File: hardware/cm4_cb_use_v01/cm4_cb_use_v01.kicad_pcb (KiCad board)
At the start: 2 copper layers, 60 x 55 mm, 21 parts, among them J1 DNP, J2 USB4105-GF-A, J3 SM04B-SRSS-TB(LF)(SN), J4 USB_OTG, U1 74LVC1G07SE-7, U2 TPD2EUSB30

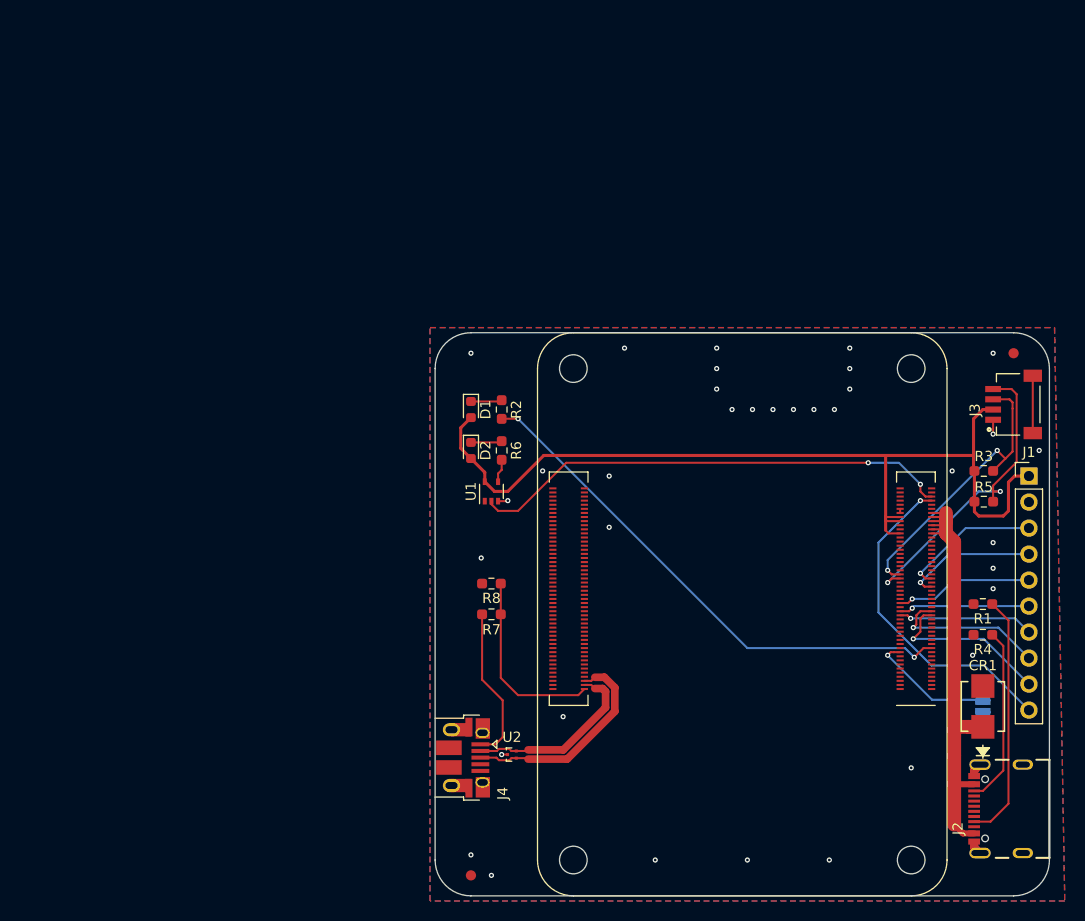
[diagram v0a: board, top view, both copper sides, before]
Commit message: added some 3d models
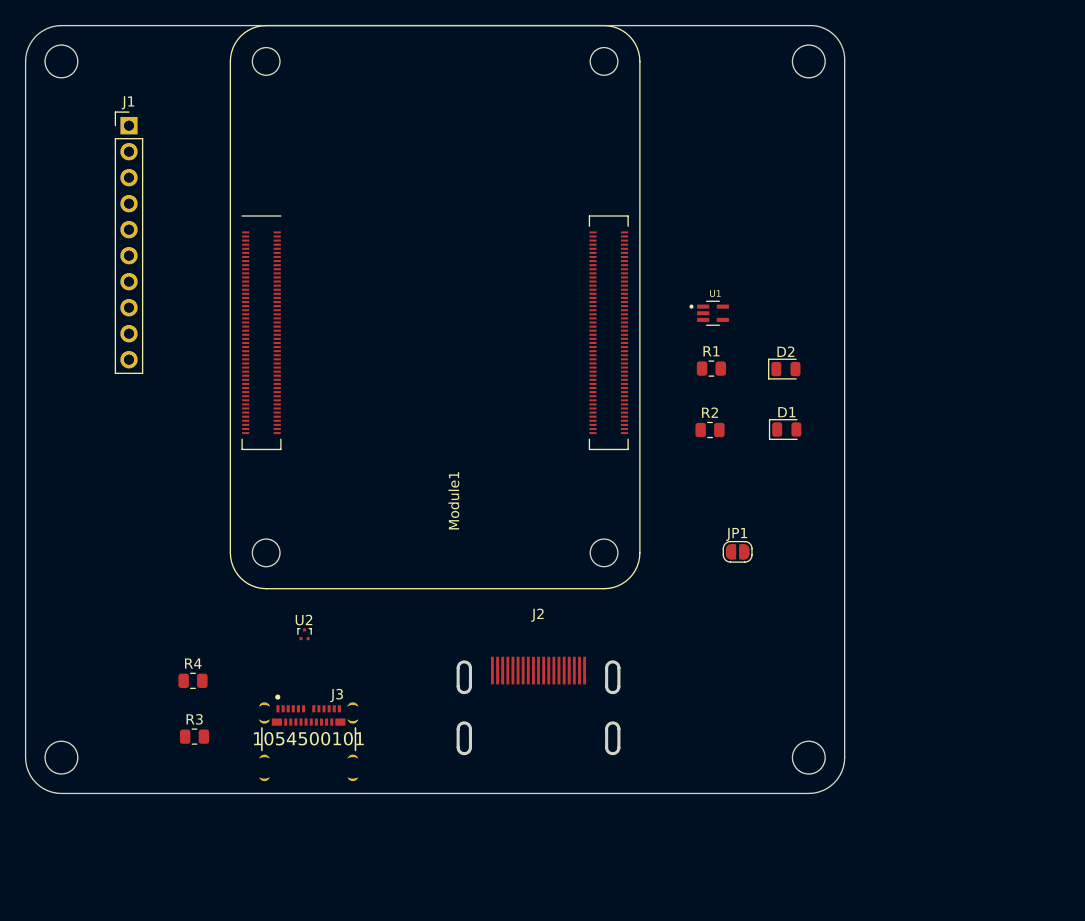
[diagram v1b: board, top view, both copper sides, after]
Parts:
- removed CR1: SMBJ5.0A-TR, footprints:SMBJ5.0A-TR
- removed J4: USB_OTG, CM4IO:USB_Micro-B_EDAC_UCON00686
- removed R5: DNP, Resistor_SMD:R_0603_1608Metric_Pad0.98x0.95mm_HandSolder
- removed R6: 1k, Resistor_SMD:R_0603_1608Metric_Pad0.98x0.95mm_HandSolder
- removed R7, R8: 2.2K 1%, Resistor_SMD:R_0603_1608Metric_Pad0.98x0.95mm_HandSolder
- removed the REF** at (120.0, 131.5)
- removed the REF** at (173.0, 80.5)
- added REF**: MountingHole_3.2mm_M3, MountingHole:MountingHole_3.2mm_M3, F.Cu at (153.0, 52.0)
- added REF**: MountingHole_3.2mm_M3, MountingHole:MountingHole_3.2mm_M3, F.Cu at (80.0, 120.0)
- added REF**: MountingHole_3.2mm_M3, MountingHole:MountingHole_3.2mm_M3, F.Cu at (153.0, 120.0)
- added REF**: MountingHole_3.2mm_M3, MountingHole:MountingHole_3.2mm_M3, F.Cu at (80.0, 52.0)
- D1, D2: footprint LED_SMD:LED_0603_1608Metric -> LED_SMD:LED_0805_2012Metric
- J2: value USB4105-GF-A -> HDMI_A; footprint USB4105-GF-A:GCT_USB4105-GF-A -> SFONG_HDMI:SOFNG_HDMI
- J3: value SM04B-SRSS-TB(LF)(SN) -> 1054500101; footprint SM04B-SRSS-TB_LF__SN_:JST_SM04B-SRSS-TB(LF)(SN) -> MOLEX_1054500101_usb_c:Molex-1054500101-MFG
- JP1: moved to F.Cu
- R1: value 5.1k -> 1k; footprint Resistor_SMD:R_0603_1608Metric_Pad0.98x0.95mm_HandSolder -> Resistor_SMD:R_0805_2012Metric
- R2: footprint Resistor_SMD:R_0603_1608Metric_Pad0.98x0.95mm_HandSolder -> Resistor_SMD:R_0805_2012Metric
- R3: value DNP -> 2.2k; footprint Resistor_SMD:R_0603_1608Metric_Pad0.98x0.95mm_HandSolder -> Resistor_SMD:R_0805_2012Metric
- R4: value 5.1k -> 2.2k; footprint Resistor_SMD:R_0603_1608Metric_Pad0.98x0.95mm_HandSolder -> Resistor_SMD:R_0805_2012Metric
- U1: value 74LVC1G07SE-7 -> SN74LVC1G07DCKR; footprint Package_TO_SOT_SMD:SOT-353_SC-70-5 -> SN74LVC1G07DCKR:SOT65P210X110-5N
- moved J1 94.3 mm to (86.6, 58.3)
- moved R3 81.3 mm to (93.0, 118.0)
- moved R4 77.3 mm to (92.8, 112.5), turned to 0 degrees
- moved J3 74.8 mm to (104.2, 119.0), turned to 0 degrees
- moved Module1 65.5 mm to (100.0, 100.0), turned to 0 degrees
- moved J2 48.1 mm to (126.6, 116.0), turned to 0 degrees
- moved R1 35.1 mm to (143.5, 82.0), turned to 0 degrees
- moved D2 31.8 mm to (150.8, 82.0), turned to 0 degrees
- moved D1 30.9 mm to (150.8, 88.0), turned to 0 degrees
- moved JP1 28.3 mm to (146.1, 99.9), turned to 0 degrees
- moved U1 27.8 mm to (143.6, 76.6), turned to 0 degrees
- moved U2 23.4 mm to (103.8, 108.0), turned to 0 degrees
- moved R2 20.4 mm to (143.3, 88.0), turned to 0 degrees
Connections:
- J3 pad 1: GND -> (no net)
- J3 pad 2: +3.3V -> (no net)
- J3 pad 3: /CM4 GPIO/GPIO2 -> (no net)
- J3 pad 4: /CM4 GPIO/GPIO3 -> (no net)
- Module1 pad 10: Net-(Module1-Pad10) -> unconnected-(Module1-Pad10)
- Module1 pad 100: Net-(Module1-Pad100) -> unconnected-(Module1-Pad100)
- Module1 pad 102: Net-(Module1-Pad102) -> unconnected-(Module1-Pad102)
- Module1 pad 104: Net-(Module1-Pad104) -> unconnected-(Module1-Pad104)
- Module1 pad 106: Net-(Module1-Pad106) -> unconnected-(Module1-Pad106)
- Module1 pad 109: Net-(Module1-Pad109) -> unconnected-(Module1-Pad109)
- Module1 pad 11: Net-(Module1-Pad11) -> unconnected-(Module1-Pad11)
- Module1 pad 110: Net-(Module1-Pad110) -> unconnected-(Module1-Pad110)
- Module1 pad 111: Net-(Module1-Pad111) -> unconnected-(Module1-Pad111)
- Module1 pad 112: Net-(Module1-Pad112) -> unconnected-(Module1-Pad112)
- Module1 pad 115: Net-(Module1-Pad115) -> unconnected-(Module1-Pad115)
- Module1 pad 116: Net-(Module1-Pad116) -> unconnected-(Module1-Pad116)
- Module1 pad 117: Net-(Module1-Pad117) -> unconnected-(Module1-Pad117)
- Module1 pad 118: Net-(Module1-Pad118) -> unconnected-(Module1-Pad118)
- Module1 pad 12: Net-(Module1-Pad12) -> unconnected-(Module1-Pad12)
- Module1 pad 121: Net-(Module1-Pad121) -> unconnected-(Module1-Pad121)
- Module1 pad 122: Net-(Module1-Pad122) -> unconnected-(Module1-Pad122)
- Module1 pad 123: Net-(Module1-Pad123) -> unconnected-(Module1-Pad123)
- Module1 pad 124: Net-(Module1-Pad124) -> unconnected-(Module1-Pad124)
- Module1 pad 127: Net-(Module1-Pad127) -> unconnected-(Module1-Pad127)
- Module1 pad 128: Net-(Module1-Pad128) -> unconnected-(Module1-Pad128)
- Module1 pad 129: Net-(Module1-Pad129) -> unconnected-(Module1-Pad129)
- Module1 pad 130: Net-(Module1-Pad130) -> unconnected-(Module1-Pad130)
- Module1 pad 133: Net-(Module1-Pad133) -> unconnected-(Module1-Pad133)
- Module1 pad 134: Net-(Module1-Pad134) -> unconnected-(Module1-Pad134)
- Module1 pad 135: Net-(Module1-Pad135) -> unconnected-(Module1-Pad135)
- Module1 pad 136: Net-(Module1-Pad136) -> unconnected-(Module1-Pad136)
- Module1 pad 139: Net-(Module1-Pad139) -> unconnected-(Module1-Pad139)
- Module1 pad 140: Net-(Module1-Pad140) -> unconnected-(Module1-Pad140)
- Module1 pad 141: Net-(Module1-Pad141) -> unconnected-(Module1-Pad141)
- Module1 pad 142: Net-(Module1-Pad142) -> unconnected-(Module1-Pad142)
- Module1 pad 143: Net-(Module1-Pad143) -> unconnected-(Module1-Pad143)
- Module1 pad 145: Net-(Module1-Pad145) -> unconnected-(Module1-Pad145)
- Module1 pad 146: Net-(Module1-Pad146) -> unconnected-(Module1-Pad146)
- Module1 pad 147: Net-(Module1-Pad147) -> unconnected-(Module1-Pad147)
- Module1 pad 148: Net-(Module1-Pad148) -> unconnected-(Module1-Pad148)
- Module1 pad 149: Net-(Module1-Pad149) -> unconnected-(Module1-Pad149)
- Module1 pad 15: Net-(Module1-Pad15) -> unconnected-(Module1-Pad15)
- Module1 pad 151: Net-(Module1-Pad151) -> /CM4 High Speed/HDMI0_CEC
- Module1 pad 152: Net-(Module1-Pad152) -> unconnected-(Module1-Pad152)
- Module1 pad 153: Net-(Module1-Pad153) -> /CM4 High Speed/HDMI0_HOTPLUG
- Module1 pad 154: Net-(Module1-Pad154) -> unconnected-(Module1-Pad154)
- Module1 pad 157: Net-(Module1-Pad157) -> unconnected-(Module1-Pad157)
- Module1 pad 158: Net-(Module1-Pad158) -> unconnected-(Module1-Pad158)
- Module1 pad 159: Net-(Module1-Pad159) -> unconnected-(Module1-Pad159)
- Module1 pad 16: Net-(Module1-Pad16) -> unconnected-(Module1-Pad16)
- Module1 pad 160: Net-(Module1-Pad160) -> unconnected-(Module1-Pad160)
- Module1 pad 163: Net-(Module1-Pad163) -> unconnected-(Module1-Pad163)
- Module1 pad 164: Net-(Module1-Pad164) -> unconnected-(Module1-Pad164)
- Module1 pad 165: Net-(Module1-Pad165) -> unconnected-(Module1-Pad165)
- Module1 pad 166: Net-(Module1-Pad166) -> unconnected-(Module1-Pad166)
- Module1 pad 169: Net-(Module1-Pad169) -> unconnected-(Module1-Pad169)
- Module1 pad 17: Net-(Module1-Pad17) -> unconnected-(Module1-Pad17)
- Module1 pad 170: Net-(Module1-Pad170) -> /CM4 High Speed/HDMI0_TX2_P
- Module1 pad 171: Net-(Module1-Pad171) -> unconnected-(Module1-Pad171)
- Module1 pad 172: Net-(Module1-Pad172) -> /CM4 High Speed/HDMI0_TX2_N
- Module1 pad 175: Net-(Module1-Pad175) -> unconnected-(Module1-Pad175)
- Module1 pad 176: Net-(Module1-Pad176) -> /CM4 High Speed/HDMI0_TX1_P
- Module1 pad 177: Net-(Module1-Pad177) -> unconnected-(Module1-Pad177)
- Module1 pad 178: Net-(Module1-Pad178) -> /CM4 High Speed/HDMI0_TX1_N
- Module1 pad 18: Net-(Module1-Pad18) -> unconnected-(Module1-Pad18)
- Module1 pad 181: Net-(Module1-Pad181) -> unconnected-(Module1-Pad181)
- Module1 pad 182: Net-(Module1-Pad182) -> /CM4 High Speed/HDMI0_TX0_P
- Module1 pad 183: Net-(Module1-Pad183) -> unconnected-(Module1-Pad183)
- Module1 pad 184: Net-(Module1-Pad184) -> /CM4 High Speed/HDMI0_TX0_N
- Module1 pad 187: Net-(Module1-Pad187) -> unconnected-(Module1-Pad187)
- Module1 pad 188: Net-(Module1-Pad188) -> /CM4 High Speed/HDMI0_CLK_P
- Module1 pad 189: Net-(Module1-Pad189) -> unconnected-(Module1-Pad189)
- Module1 pad 19: Net-(Module1-Pad19) -> unconnected-(Module1-Pad19)
- Module1 pad 190: Net-(Module1-Pad190) -> /CM4 High Speed/HDMI0_CLK_N
- Module1 pad 193: Net-(Module1-Pad193) -> unconnected-(Module1-Pad193)
- Module1 pad 194: Net-(Module1-Pad194) -> unconnected-(Module1-Pad194)
- Module1 pad 195: Net-(Module1-Pad195) -> unconnected-(Module1-Pad195)
- Module1 pad 196: Net-(Module1-Pad196) -> unconnected-(Module1-Pad196)
- Module1 pad 199: Net-(Module1-Pad199) -> /CM4 High Speed/HDMI0_SDA
- Module1 pad 200: Net-(Module1-Pad200) -> /CM4 High Speed/HDMI0_SCL
- Module1 pad 24: Net-(Module1-Pad24) -> unconnected-(Module1-Pad24)
- Module1 pad 25: Net-(Module1-Pad25) -> unconnected-(Module1-Pad25)
- Module1 pad 26: Net-(Module1-Pad26) -> unconnected-(Module1-Pad26)
- Module1 pad 27: Net-(Module1-Pad27) -> unconnected-(Module1-Pad27)
- Module1 pad 28: Net-(Module1-Pad28) -> unconnected-(Module1-Pad28)
- Module1 pad 29: Net-(Module1-Pad29) -> unconnected-(Module1-Pad29)
- Module1 pad 3: Net-(Module1-Pad3) -> unconnected-(Module1-Pad3)
- Module1 pad 30: Net-(Module1-Pad30) -> unconnected-(Module1-Pad30)
- Module1 pad 31: Net-(Module1-Pad31) -> unconnected-(Module1-Pad31)
- Module1 pad 34: Net-(Module1-Pad34) -> unconnected-(Module1-Pad34)
- Module1 pad 35: Net-(Module1-Pad35) -> unconnected-(Module1-Pad35)
- Module1 pad 36: Net-(Module1-Pad36) -> unconnected-(Module1-Pad36)
- Module1 pad 4: Net-(Module1-Pad4) -> unconnected-(Module1-Pad4)
- Module1 pad 41: Net-(Module1-Pad41) -> unconnected-(Module1-Pad41)
- Module1 pad 45: Net-(Module1-Pad45) -> unconnected-(Module1-Pad45)
- Module1 pad 46: Net-(Module1-Pad46) -> unconnected-(Module1-Pad46)
- Module1 pad 47: Net-(Module1-Pad47) -> unconnected-(Module1-Pad47)
- Module1 pad 48: Net-(Module1-Pad48) -> unconnected-(Module1-Pad48)
- Module1 pad 49: Net-(Module1-Pad49) -> unconnected-(Module1-Pad49)
- Module1 pad 5: Net-(Module1-Pad5) -> unconnected-(Module1-Pad5)
- Module1 pad 50: Net-(Module1-Pad50) -> unconnected-(Module1-Pad50)
- Module1 pad 54: Net-(Module1-Pad54) -> unconnected-(Module1-Pad54)
- Module1 pad 57: Net-(Module1-Pad57) -> unconnected-(Module1-Pad57)
- Module1 pad 6: Net-(Module1-Pad6) -> unconnected-(Module1-Pad6)
- Module1 pad 61: Net-(Module1-Pad61) -> unconnected-(Module1-Pad61)
- Module1 pad 62: Net-(Module1-Pad62) -> unconnected-(Module1-Pad62)
- Module1 pad 63: Net-(Module1-Pad63) -> unconnected-(Module1-Pad63)
- Module1 pad 64: Net-(Module1-Pad64) -> unconnected-(Module1-Pad64)
- Module1 pad 67: Net-(Module1-Pad67) -> unconnected-(Module1-Pad67)
- Module1 pad 68: Net-(Module1-Pad68) -> unconnected-(Module1-Pad68)
- Module1 pad 69: Net-(Module1-Pad69) -> unconnected-(Module1-Pad69)
- Module1 pad 70: Net-(Module1-Pad70) -> unconnected-(Module1-Pad70)
- Module1 pad 72: Net-(Module1-Pad72) -> unconnected-(Module1-Pad72)
- Module1 pad 73: Net-(Module1-Pad73) -> unconnected-(Module1-Pad73)
- Module1 pad 75: Net-(Module1-Pad75) -> unconnected-(Module1-Pad75)
- Module1 pad 76: Net-(Module1-Pad76) -> unconnected-(Module1-Pad76)
- Module1 pad 80: Net-(Module1-Pad80) -> unconnected-(Module1-Pad80)
- Module1 pad 82: Net-(Module1-Pad82) -> unconnected-(Module1-Pad82)
- Module1 pad 89: Net-(Module1-Pad89) -> unconnected-(Module1-Pad89)
- Module1 pad 9: Net-(Module1-Pad9) -> unconnected-(Module1-Pad9)
- Module1 pad 91: Net-(Module1-Pad91) -> unconnected-(Module1-Pad91)
- Module1 pad 92: Net-(Module1-Pad92) -> unconnected-(Module1-Pad92)
- Module1 pad 94: Net-(Module1-Pad94) -> unconnected-(Module1-Pad94)
- Module1 pad 96: Net-(Module1-Pad96) -> unconnected-(Module1-Pad96)
- Module1 pad 97: Net-(Module1-Pad97) -> unconnected-(Module1-Pad97)
- Module1 pad 99: Net-(Module1-Pad99) -> unconnected-(Module1-Pad99)
- R1 pad 1: Net-(J2-PadA5) -> Net-(D2-Pad1)
- R1 pad 2: GND -> Net-(R1-Pad2)
- R3 pad 1: +3.3V -> Net-(J3-PadA4)
- R3 pad 2: /CM4 GPIO/GPIO2 -> /CM4 High Speed/USB_OTG_ID
- R4 pad 1: Net-(J2-PadB5) -> /CM4 High Speed/USB_OTG_ID
- U1 pad 4: Net-(R6-Pad2) -> Net-(R1-Pad2)
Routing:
- net +3.3V: track 89.7 -> 0.00 mm
- net /CM4 GPIO/nLED_Activity: track 52.0 -> 0.00 mm, vias 2 -> 0
- net /CM4 GPIO/nPWR_LED: track 47.3 -> 0.00 mm, vias 2 -> 0
- net +5V: track 46.9 -> 0.00 mm
- net /CM4 GPIO/nRPIBOOT: track 32.4 -> 0.00 mm, vias 1 -> 0
- net /CM4 GPIO/GPIO3: track 30.7 -> 0.00 mm, vias 2 -> 0
- net /CM4 GPIO/GPIO2: track 28.2 -> 0.00 mm, vias 2 -> 0
- net Net-(J2-PadA5): track 24.2 -> 0.00 mm
- net /CM4 High Speed/USB2_P: track 21.1 -> 0.00 mm
- net /CM4 High Speed/USB_OTG_ID: track 18.3 -> 0.00 mm
- net /CM4 High Speed/USB2_N: track 18.1 -> 0.00 mm
- net Net-(J2-PadB5): track 17.4 -> 0.00 mm
- net /CM4 GPIO/GPIO7: track 16.6 -> 0.00 mm, vias 1 -> 0
- net /CM4 GPIO/GPIO8: track 15.5 -> 0.00 mm, vias 1 -> 0
- net Net-(J4-Pad1): track 15.3 -> 0.00 mm
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- removed copper zone on B.Cu, net GND
- removed copper zone on F.Cu, net GND
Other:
- board size 60 x 55 mm -> 80 x 75 mm
- board text removed: "RPi CM4 Base Carrier"
- board text removed: "Receptacle component options: 1.5mm height: 2x Hirose DF40C-100DS-0.4v OR 3.0mm height: 2x Hirose DF40HC(3.0)-100DS-0.4v"
- board text removed: "Wireless Keepout"
- board text removed: "v01"

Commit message: added 3d models and started pcb layout
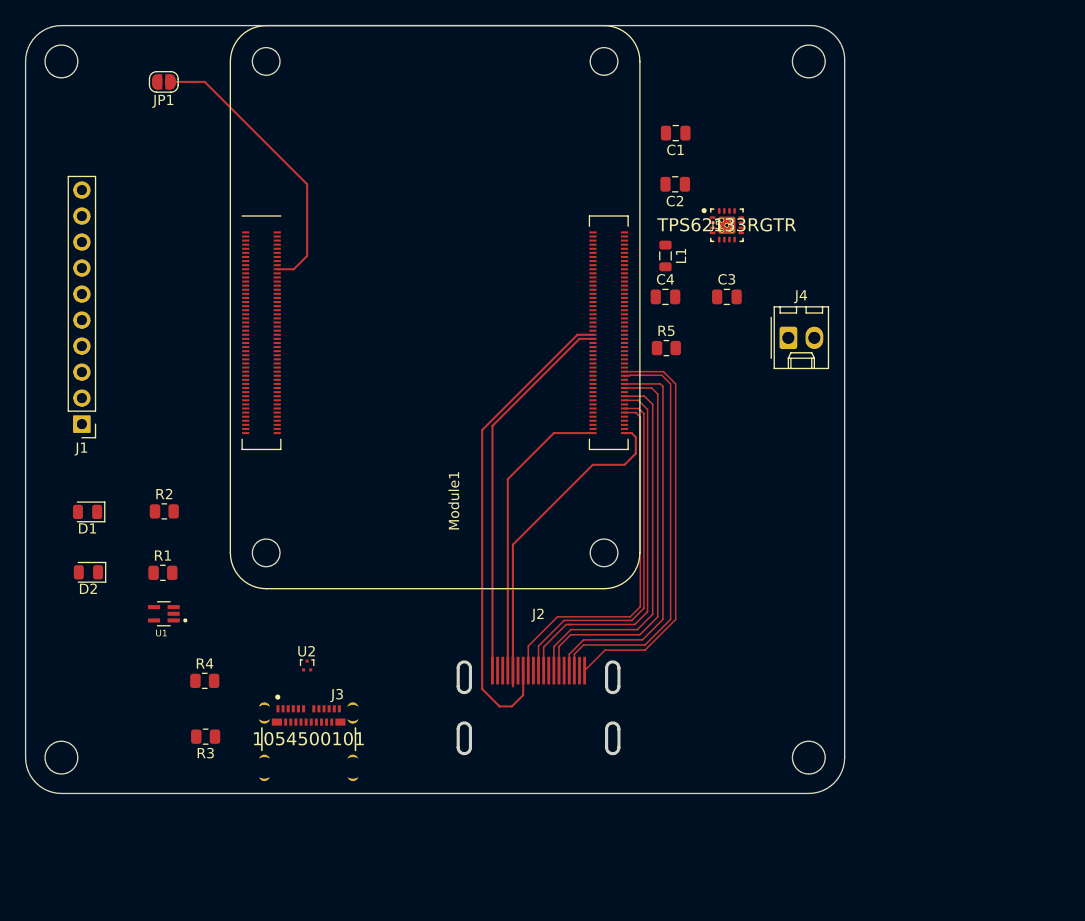
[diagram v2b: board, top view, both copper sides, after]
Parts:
- added C1: 10uF, Capacitor_SMD:C_0805_2012Metric, F.Cu at (140.0, 59.0)
- added C2: 0.1uF, Capacitor_SMD:C_0805_2012Metric, F.Cu at (139.9, 64.0)
- added C3: 3.3nF, Capacitor_SMD:C_0805_2012Metric, F.Cu at (145.0, 75.0)
- added C4: 22uF, Capacitor_SMD:C_0805_2012Metric, F.Cu at (139.0, 75.0)
- added J4: molex_5046_2pin, Connector_Molex:Molex_KK-254_AE-6410-02A_1x02_P2.54mm_Vertical, F.Cu at (151.0, 79.0)
- added J5: TPS62133RGTR, TPS62133:Texas_Instruments-TPS62133RGTR-Manufacturer_Recommended, F.Cu at (145.0, 68.0)
- added L1: 2.2uH, Inductor_SMD:L_0805_2012Metric, F.Cu at (139.0, 71.0)
- added R5: 100K, Resistor_SMD:R_0805_2012Metric, F.Cu at (139.1, 80.0)
- moved JP1 72.4 mm to (90.0, 54.0), turned to 180 degrees
- moved D2 71.0 mm to (82.6, 101.9), turned to 180 degrees
- moved D1 68.8 mm to (82.5, 96.0), turned to 180 degrees
- moved U1 61.1 mm to (90.0, 106.0), turned to 180 degrees
- moved R1 57.2 mm to (89.9, 102.0)
- moved R2 53.9 mm to (90.0, 96.0)
- moved J1 29.5 mm to (82.0, 87.4), turned to 180 degrees
- moved U2 3.06 mm to (104.0, 111.0)
- moved R4 1.15 mm to (94.0, 112.5)
- moved R3 1.09 mm to (94.1, 118.0), turned to 180 degrees
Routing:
- net /CM4 High Speed/HDMI0_CEC: track 0.00 -> 47.5 mm
- net /CM4 High Speed/HDMI0_TX2_N: track 0.00 -> 40.3 mm
- net /CM4 High Speed/HDMI0_TX2_P: track 0.00 -> 39.5 mm
- net /CM4 High Speed/HDMI0_TX1_P: track 0.00 -> 38.9 mm
- net /CM4 High Speed/HDMI0_TX1_N: track 0.00 -> 38.4 mm
- net /CM4 High Speed/HDMI0_HOTPLUG: track 0.00 -> 37.2 mm
- net /CM4 High Speed/HDMI0_TX0_P: track 0.00 -> 36.9 mm
- net /CM4 High Speed/HDMI0_TX0_N: track 0.00 -> 36.5 mm
- net /CM4 High Speed/HDMI0_CLK_P: track 0.00 -> 35.3 mm
- net /CM4 High Speed/HDMI0_CLK_N: track 0.00 -> 35.2 mm
- net /CM4 High Speed/HDMI0_SCL: track 0.00 -> 32.4 mm
- net /CM4 High Speed/HDMI0_SDA: track 0.00 -> 28.9 mm
- net /CM4 GPIO/EEPROM_nWP: track 0.00 -> 28.0 mm

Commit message: First draft done
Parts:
- added REF**: Fiducial_1mm_Mask2mm, Fiducial:Fiducial_1mm_Mask2mm, F.Cu at (148.0, 120.0)
- added REF**: Fiducial_1mm_Mask2mm, Fiducial:Fiducial_1mm_Mask2mm, F.Cu at (85.0, 52.0)
- added REF**: Fiducial_1mm_Mask2mm, Fiducial:Fiducial_1mm_Mask2mm, F.Cu at (148.0, 52.0)
- added REF**: Fiducial_1mm_Mask2mm, Fiducial:Fiducial_1mm_Mask2mm, F.Cu at (85.0, 120.0)
- moved C1 21.1 mm to (152.8, 75.8), turned to 0 degrees
- moved C2 14.5 mm to (152.8, 70.8), turned to 0 degrees
- moved JP1 14.1 mm to (99.5, 64.4)
- moved R3 9.65 mm to (101.8, 112.1)
- moved R4 9.08 mm to (101.7, 107.7)
- moved U2 3.70 mm to (107.7, 111.3)
- moved J4 3.34 mm to (152.4, 82.0), turned to -90 degrees
- moved C4 0.90 mm to (139.9, 75.0)
- moved L1 0.90 mm to (139.9, 71.0), turned to 180 degrees
- moved R5 0.81 mm to (139.9, 80.0)
- moved J3 0.50 mm to (104.1, 119.5)
- moved J2 0.39 mm to (126.6, 116.4)
- moved C3 0.29 mm to (145.3, 75.0), turned to 180 degrees
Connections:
- net Net-(C1-Pad1) renamed +7.4V
- J5 pad 14: unconnected-(J5-Pad14) -> +5V
- Module1 pad 86: +3.3V -> unconnected-(Module1-Pad86)
- Module1 pad 88: +1.8V -> unconnected-(Module1-Pad88)
- Module1 pad 90: +1.8V -> unconnected-(Module1-Pad90)
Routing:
- net +5V: track 0.00 -> 169.4 mm, vias 0 -> 3
- net /CM4 High Speed/USB2_N: track 0.00 -> 63.0 mm, vias 0 -> 2
- net /CM4 High Speed/USB2_P: track 0.00 -> 62.5 mm
- net /CM4 High Speed/USB_OTG_ID: track 0.00 -> 58.2 mm
- net +3.3V: track 0.00 -> 53.7 mm, vias 0 -> 1
- net /CM4 GPIO/nRPIBOOT: track 0.00 -> 49.5 mm, vias 0 -> 2
- net /CM4 GPIO/nLED_Activity: track 0.00 -> 40.4 mm, vias 0 -> 4
- net /CM4 GPIO/GPIO10: track 0.00 -> 31.1 mm
- net /CM4 GPIO/GPIO9: track 0.00 -> 29.9 mm
- net /CM4 GPIO/GPIO11: track 0.00 -> 29.0 mm
- net /CM4 GPIO/nPWR_LED: track 0.00 -> 23.4 mm
- net +7.4V: track 0.00 -> 21.3 mm
- net /CM4 GPIO/GPIO7: track 0.00 -> 19.7 mm, vias 0 -> 2
- net /CM4 GPIO/GPIO8: track 0.00 -> 18.8 mm, vias 0 -> 2
- net /CM4 GPIO/GPIO14: track 0.00 -> 17.2 mm
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- added copper zone on B.Cu, net GND
- added copper zone on F.Cu, net GND

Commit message: updated
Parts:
- removed the REF** at (148.0, 120.0)
- removed the REF** at (85.0, 52.0)
- removed the REF** at (148.0, 52.0)
- removed the REF** at (85.0, 120.0)
- added R6: 262K, Resistor_SMD:R_0805_2012Metric, F.Cu at (147.0, 92.0)
- added R7: 50K, Resistor_SMD:R_0805_2012Metric, F.Cu at (147.0, 94.3)
- added SW1: SW_SPDT, c&k_slide_switch_1101M2S3AQE2:c&k_slide_switch_1101M2S3AQE2, F.Cu at (141.8, 121.8)
- J2: footprint SFONG_HDMI:SOFNG_HDMI -> MOLEX_1054500101_usb_c:molex_hdmi
- moved D1 28.2 mm to (95.0, 121.3), turned to -90 degrees
- moved D2 25.6 mm to (99.3, 121.3), turned to -90 degrees
- moved C2 22.7 mm to (152.0, 93.5), turned to 180 degrees
- moved R2 21.4 mm to (95.0, 116.8), turned to 90 degrees
- moved J5 20.7 mm to (152.1, 87.5)
- moved C1 20.1 mm to (152.0, 95.9), turned to 180 degrees
- moved J4 19.2 mm to (152.0, 101.2)
- moved L1 18.1 mm to (147.1, 87.6)
- moved R1 17.6 mm to (99.4, 116.8), turned to 90 degrees
- moved C3 17.4 mm to (152.0, 91.1)
- moved C4 12.6 mm to (147.0, 85.4)
- moved R5 12.0 mm to (147.0, 89.7)
- moved U1 11.1 mm to (100.6, 109.3), turned to -90 degrees
- moved R4 4.79 mm to (105.8, 110.2)
- moved R3 4.21 mm to (105.8, 113.4)
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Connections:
- J4 pad 1: +7.4V -> Net-(J4-Pad1)
- J5 pad 5: GND -> Net-(J5-Pad5)
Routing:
- net +5V: track 169.4 -> 133.7 mm, vias 3 -> 2
- net +7.4V: track 21.3 -> 46.3 mm
- net /CM4 GPIO/nLED_Activity: track 40.4 -> 59.5 mm
- net +3.3V: track 53.7 -> 72.7 mm, vias 1 -> 2
- net /CM4 High Speed/HDMI0_CEC: track 55.4 -> 38.3 mm, vias 0 -> 2
- net Net-(J4-Pad1): track 0.00 -> 17.0 mm
- net /CM4 High Speed/USB2_N: track 63.0 -> 74.6 mm
- net Net-(J5-Pad4): track 12.9 -> 3.40 mm
- net Net-(J5-Pad5): track 0.00 -> 8.31 mm
- net /CM4 High Speed/HDMI0_CLK_N: track 39.4 -> 31.7 mm
- net /CM4 High Speed/USB2_P: track 62.5 -> 69.7 mm
- net /CM4 High Speed/USB_OTG_ID: track 58.2 -> 64.2 mm
- net /CM4 High Speed/HDMI0_SDA: track 27.8 -> 33.4 mm
- net Net-(J5-Pad1): track 8.45 -> 3.64 mm
- net Net-(C3-Pad1): track 7.93 -> 4.17 mm
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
